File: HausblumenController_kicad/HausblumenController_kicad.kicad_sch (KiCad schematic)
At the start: 3 parts, among them Q1 IRLML2402, U1 BlackPill_40pin_SWD

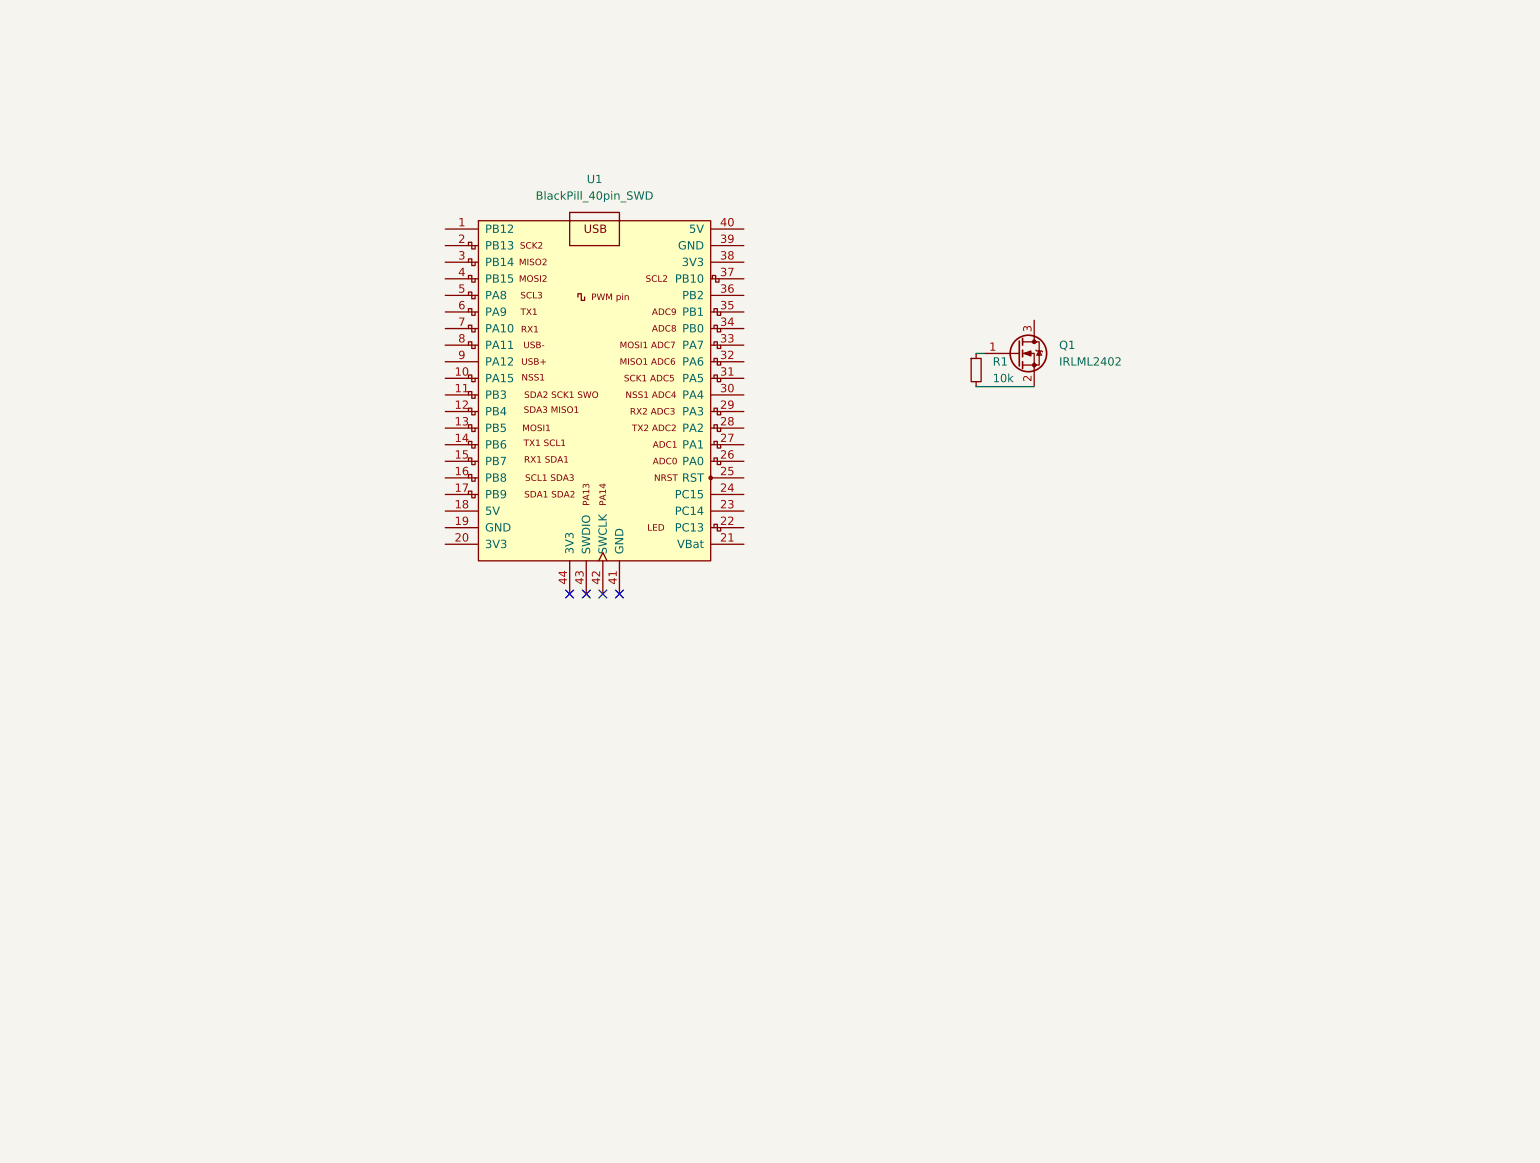
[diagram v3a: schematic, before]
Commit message: added components on schemes
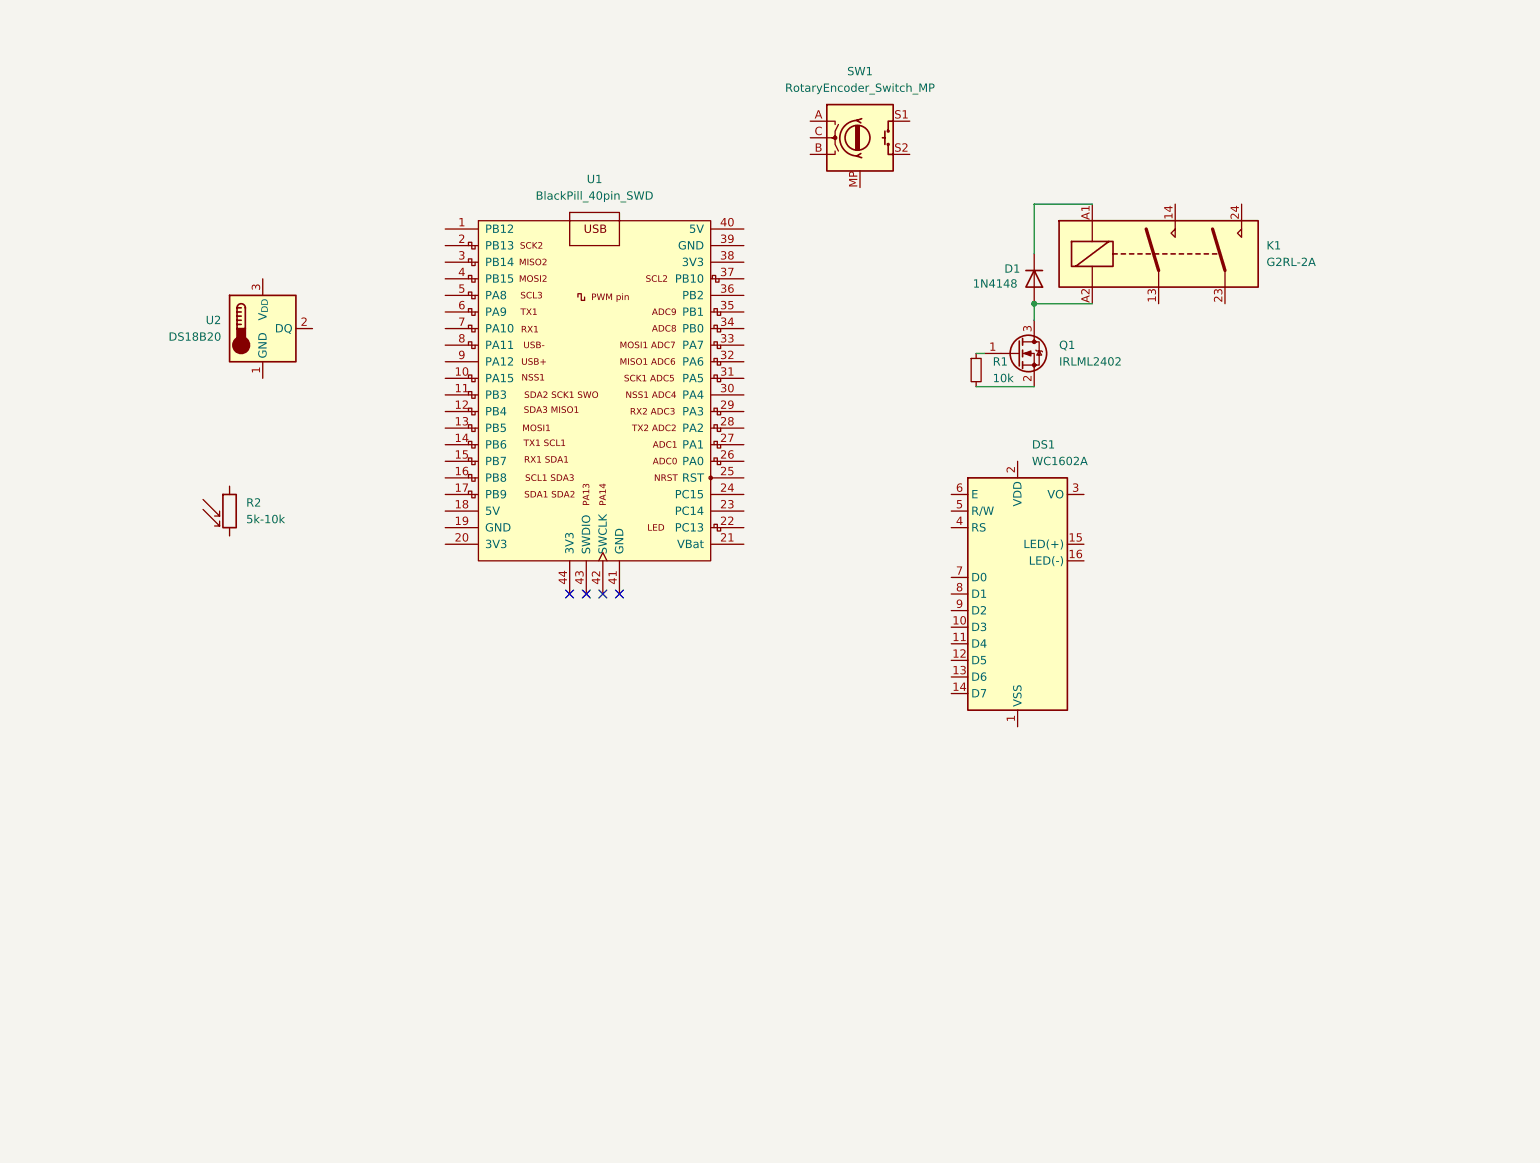
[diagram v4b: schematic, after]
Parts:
- added D1: 1N4148, Diode_THT:D_DO-35_SOD27_P7.62mm_Horizontal, symbol Diode:1N4148
- added DS1: WC1602A, Display:WC1602A, symbol Display_Character:WC1602A
- added K1: G2RL-2A, Relay_THT:Relay_DPST_Omron_G2RL-2A, symbol Relay:G2RL-2A
- added R2: 5k-10k, OptoDevice:R_LDR_5.1x4.3mm_P3.4mm_Vertical, symbol Device:R_Photo
- added SW1: RotaryEncoder_Switch_MP, Rotary_Encoder:RotaryEncoder_Alps_EC12E-Switch_Vertical_H20mm, symbol Device:RotaryEncoder_Switch_MP
- added U2: DS18B20, Package_TO_SOT_THT:TO-92_Inline, symbol Sensor_Temperature:DS18B20
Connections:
- net at Q1.3 (D): now also D1.2 (A), K1.A2
- new net: D1.1 (K), K1.A1

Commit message: feat: added powerbus
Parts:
- added R3: 10k, Resistor_SMD:R_0603_1608Metric, symbol Device:R_Small
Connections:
- net AGND: now reaches U2.1 (GND)
- net AGND: now also DS1.1 (VSS), U1.19 (GND), U1.39 (GND), R3.2
- net +3V3: now reaches U2.3 (V_{DD})
- net +3V3: now also DS1.2 (VDD), R2.1, U1.20 (3V3), U1.38 (3V3)
- net +12V: now reaches K1.14
- net +12V: now also D1.1 (K), K1.A1
- net at R2.2: now also R3.1
- no-connect marks 4 -> 5

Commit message: feat: added functional components
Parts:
- added D2, D3: 1N4148, Diode_THT:D_DO-35_SOD27_P7.62mm_Horizontal, symbol Diode:1N4148
- added K2, K3: G2RL-2A, Relay_THT:Relay_DPST_Omron_G2RL-2A, symbol Relay:G2RL-2A
- added Q2, Q3: IRLML2402, Package_TO_SOT_SMD:SOT-23, symbol Transistor_FET:IRLML2060
- added R4, R5: 10k, Resistor_SMD:R_0603_1608Metric, symbol Device:R_Small
- added U3: DHT11, Sensor:Aosong_DHT11_5.5x12.0_P2.54mm, symbol Sensor:DHT11
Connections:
- net +12V: now also D2.1 (K), D3.1 (K), K2.14, K2.A1, K3.14, K3.A1
- net +3V3: now also U3.1 (VDD)
- net AGND: now also U3.4 (GND)
- new net: Q3.1 (G), R5.1
- new net: Q3.2 (S), R5.2
- new net: D3.2 (A), K3.A2, Q3.3 (D)
- new net: D2.2 (A), K2.A2, Q2.3 (D)
- new net: Q2.1 (G), R4.1
- new net: Q2.2 (S), R4.2
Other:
- note added: "Control"
- note added: "Light"
- note added: "Show"
- note added: "Steam"
- note added: "Water"
- moved on the sheet: D1, DS1, K1, Q1, R1, R2, R3, SW1, U2

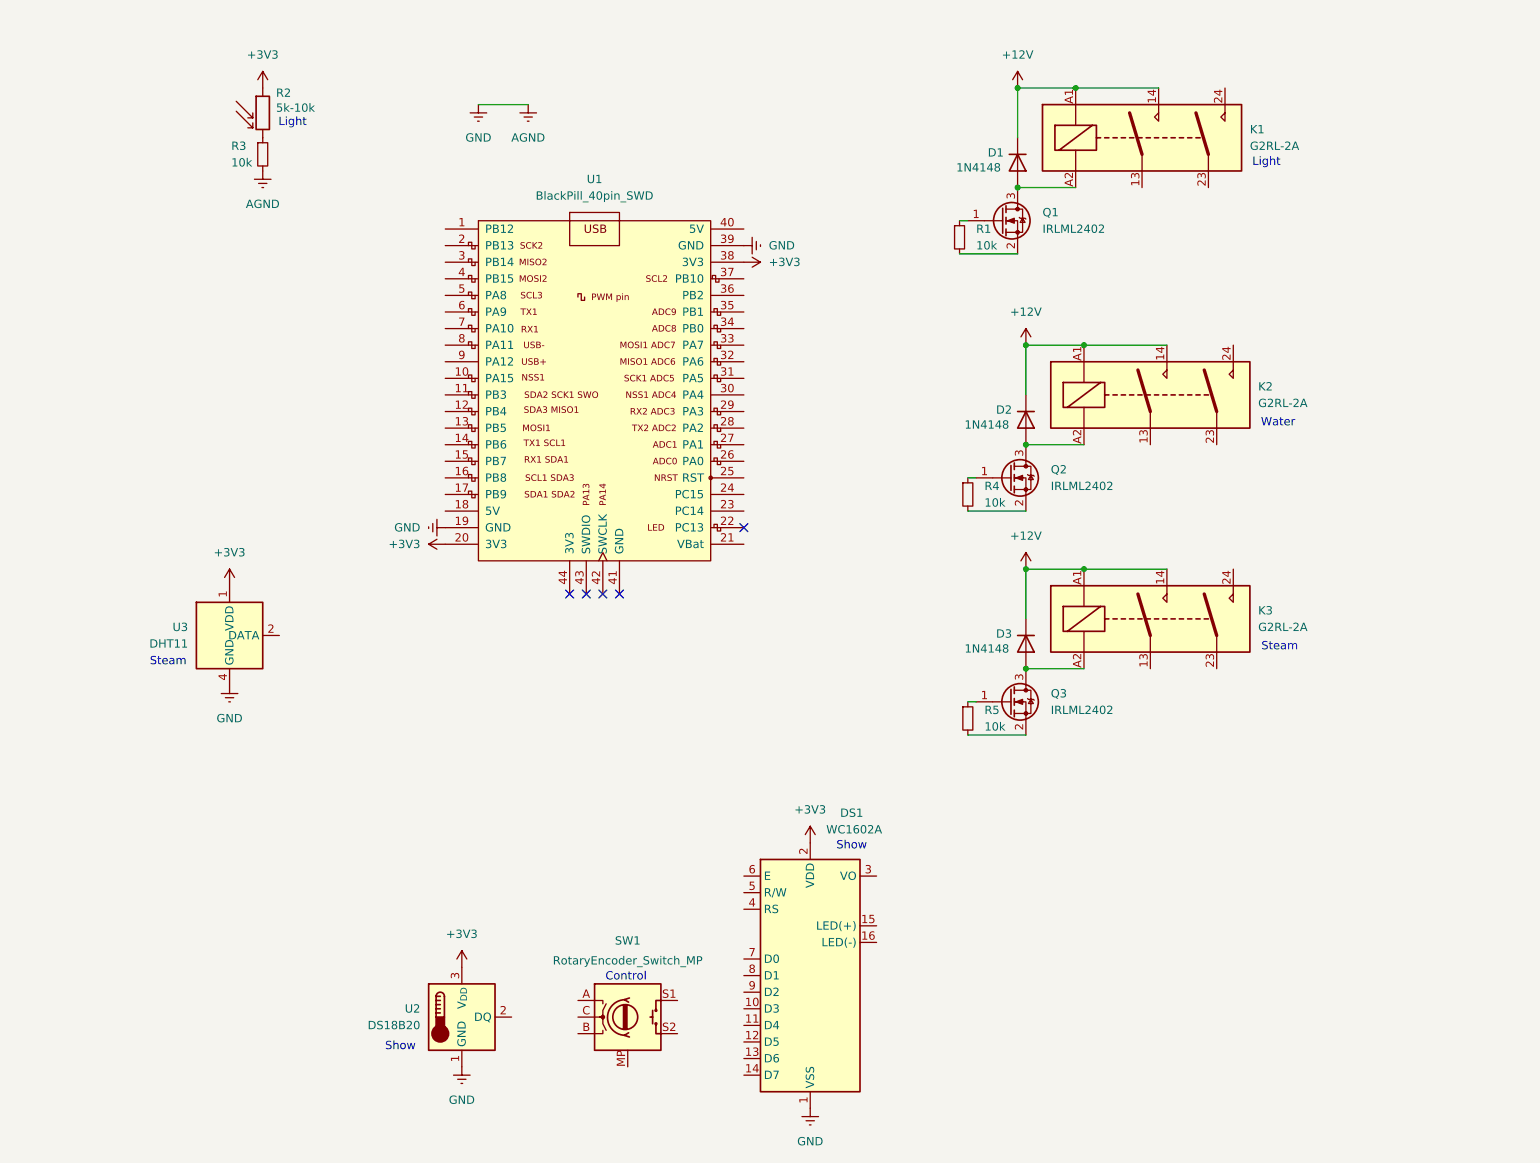
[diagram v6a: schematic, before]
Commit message: create CubeMX project
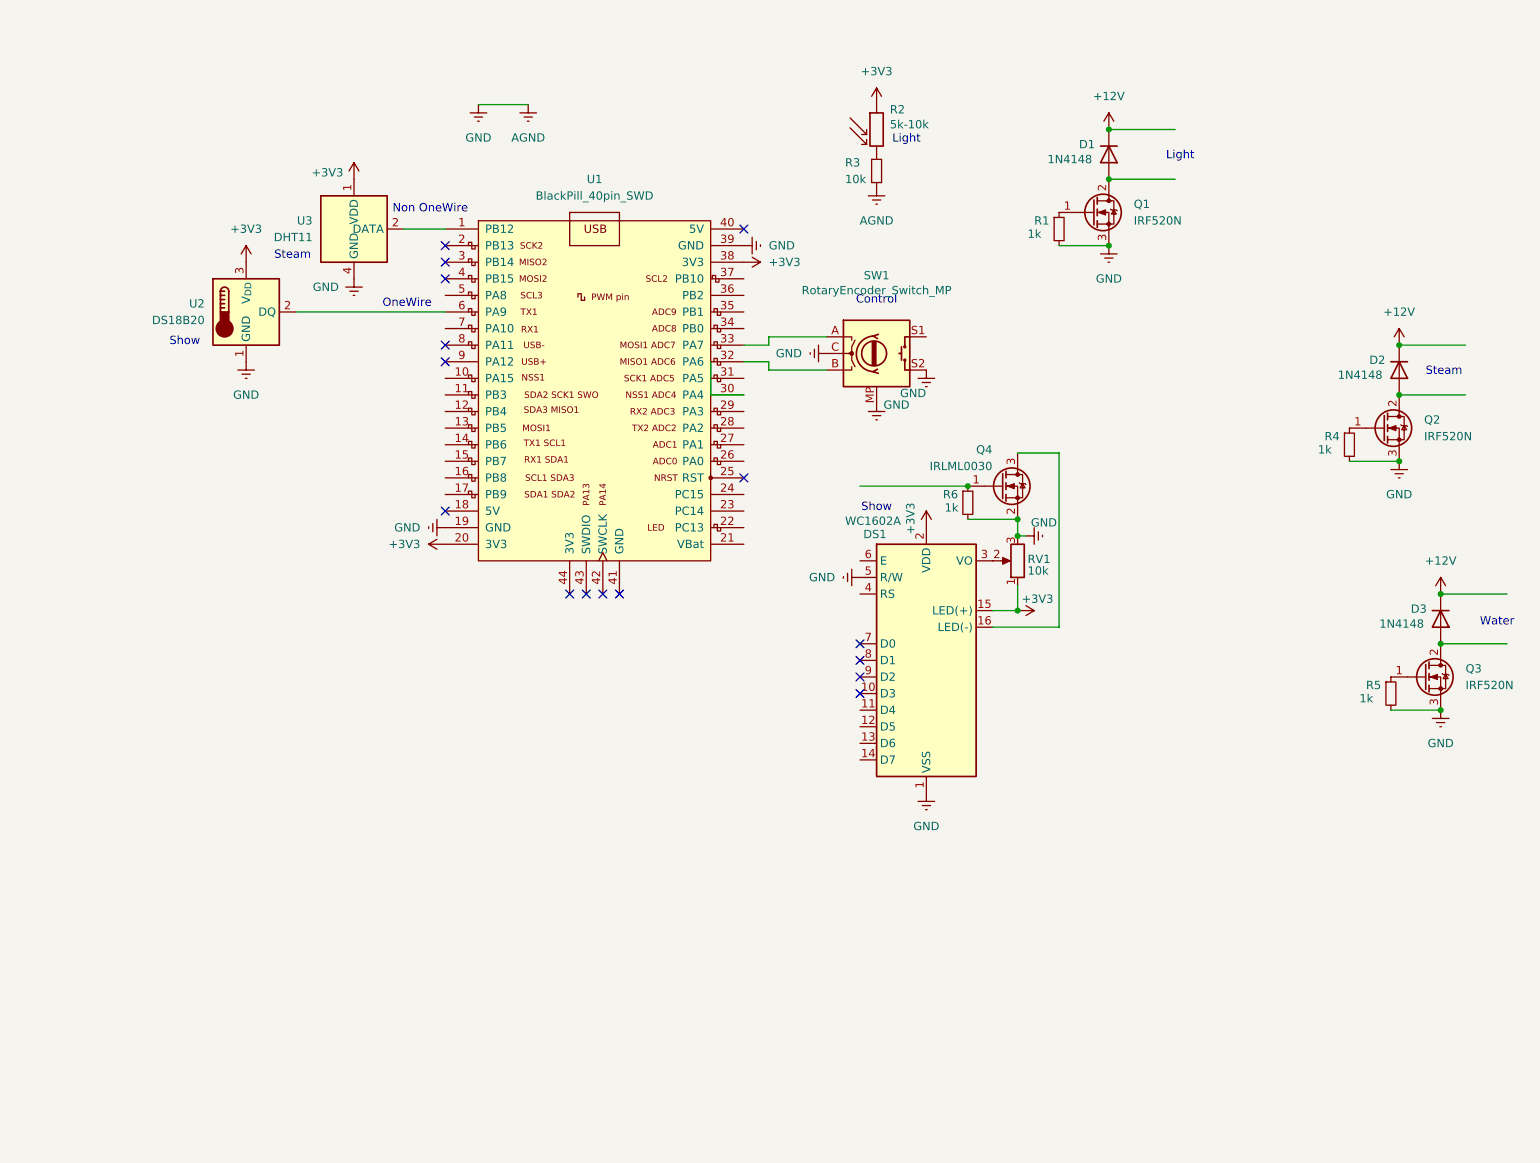
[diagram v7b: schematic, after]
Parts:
- removed K1, K2, K3: G2RL-2A, Relay_THT:Relay_DPST_Omron_G2RL-2A, symbol Relay:G2RL-2A
- removed Q1, Q2, Q3: IRLML2402, Package_TO_SOT_SMD:SOT-23, symbol Transistor_FET:IRLML2060
- added Q1, Q2, Q3: IRF520N, Package_TO_SOT_THT:TO-220-3_Vertical, symbol Transistor_FET:IRF540N
- added Q4: IRLML0030, Package_TO_SOT_SMD:SOT-23, symbol Transistor_FET:IRLML0030
- added R6: 1k, Resistor_SMD:R_0603_1608Metric, symbol Device:R_Small
- added RV1: 10k, symbol Device:R_Potentiometer
- R1, R4, R5: value 10k -> 1k
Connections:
- net +3V3: now also DS1.15 (LED(+)), RV1.1
- net AGND: now also DS1.5 (R/W), R1.2, R4.2, R5.2, SW1.C, SW1.MP, SW1.S2, Q1.3 (S), Q2.3 (S), Q3.3 (S), Q4.2 (S), R6.2, RV1.3
- net at U2.2 (DQ): now also U1.6 (PA9)
- net at U1.1 (PB12): now also U3.2 (DATA)
- net at U1.32 (PA6): now also SW1.B
- net at U1.33 (PA7): now also SW1.A
- net at D1.2 (A): now also Q1.2 (D)
- net at R5.1: now also Q3.1 (G)
- net at D3.2 (A): now also Q3.2 (D)
- net at R1.1: now also Q1.1 (G)
- net at D2.2 (A): now also Q2.2 (D)
- net at DS1.16 (LED(-)): now also Q4.3 (D)
- net at DS1.3 (VO): now also RV1.2
- net at R4.1: now also Q2.1 (G)
- new net: Q4.1 (G), R6.1
- no-connect marks 5 -> 16
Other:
- note added: "Non OneWire"
- note added: "OneWire"
- moved on the sheet: D1, DS1, R1, R2, R3, SW1, U2, U3
